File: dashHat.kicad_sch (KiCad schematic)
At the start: 26 parts, among them J1 Input, J2 LCD, J3 GPIO, J4 LEDs, Q1 BSS138, Q10 ADP197, Q2 BSS138, U1 CAT24C256

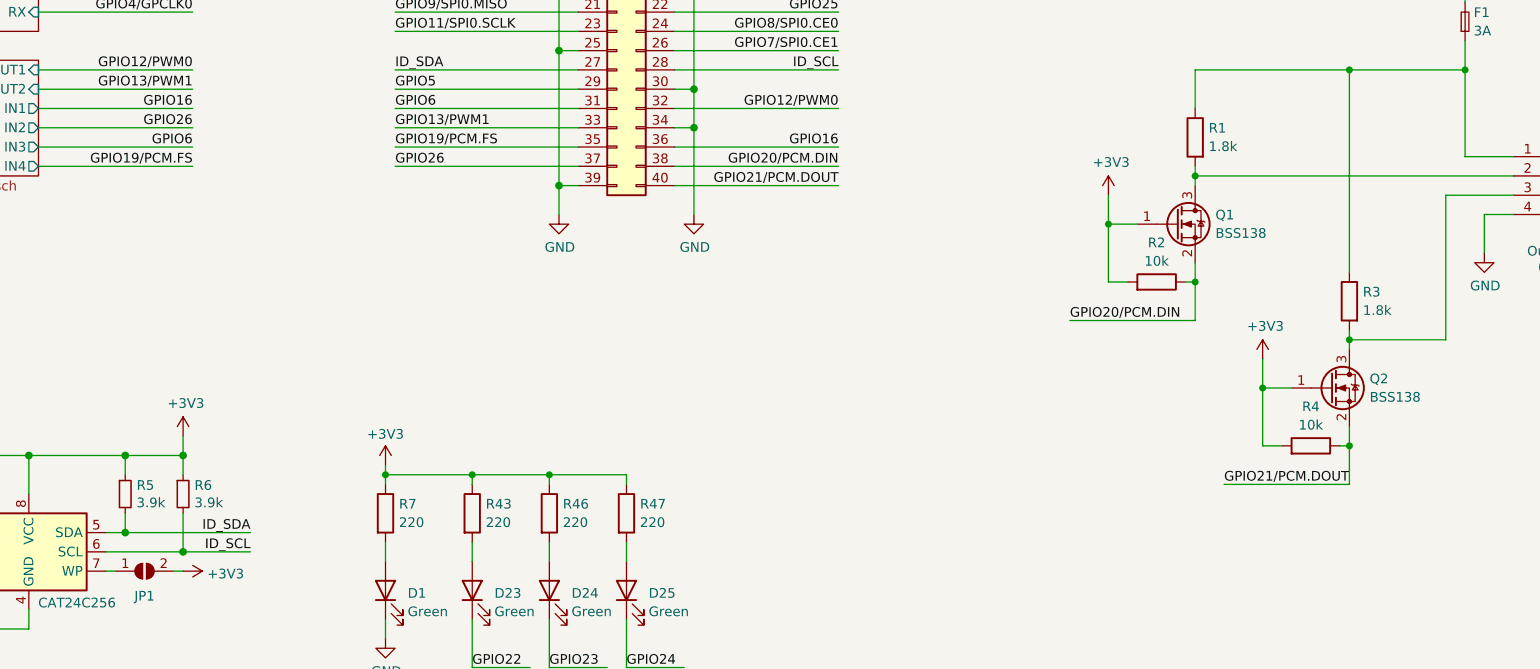
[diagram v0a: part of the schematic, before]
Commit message: update resistors to more commmon values
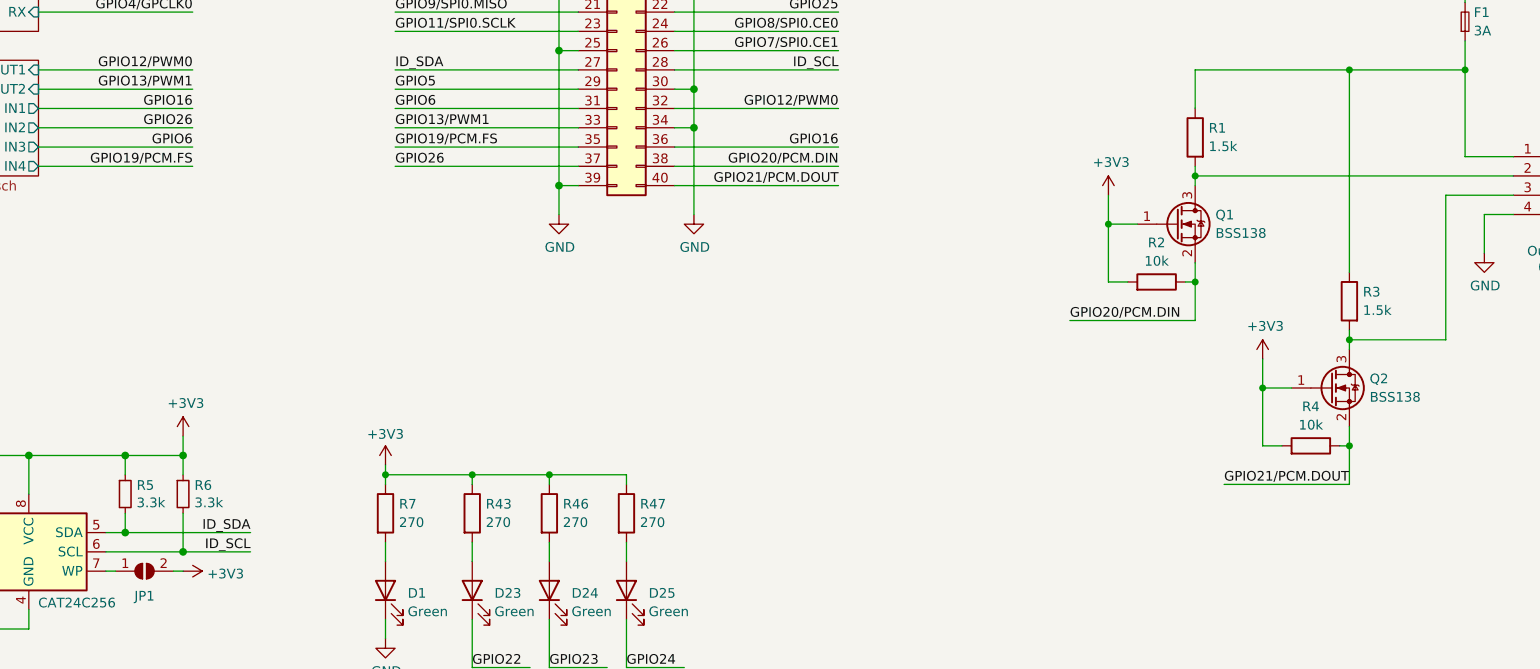
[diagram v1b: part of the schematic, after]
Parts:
- R1, R3: value 1.8k -> 1.5k
- R43, R46, R47, R7: value 220 -> 270
- R5, R6: value 3.9k -> 3.3k
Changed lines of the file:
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@@
 			)
 		)
-		(property "Value" "220"
+		(property "Value" "270"
 			(at 127.508 161.2321 0)
 			(effects
@@
 			)
 		)
-		(property "Value" "3.9k"
+		(property "Value" "3.3k"
 			(at 81.5087 158.6293 0)
 			(effects
@@
 			)
 		)
-		(property "Value" "220"
+		(property "Value" "270"
 			(at 147.828 161.2321 0)
 			(effects
@@
 			)
 		)
-		(property "Value" "1.8k"
+		(property "Value" "1.5k"
 			(at 222.758 111.7021 0)
 			(effects
@@
 			)
 		)
-		(property "Value" "3.9k"
+		(property "Value" "3.3k"
 			(at 89.1287 158.6293 0)
 			(effects
@@
 			)
 		)
-		(property "Value" "220"
+		(property "Value" "270"
 			(at 116.078 161.2321 0)
 			(effects
@@
 			)
 		)
-		(property "Value" "220"
+		(property "Value" "270"
 			(at 137.668 161.2321 0)
 			(effects
@@
 			)
 		)
-		(property "Value" "1.8k"
+		(property "Value" "1.5k"
 			(at 243.078 133.2921 0)
 			(effects
